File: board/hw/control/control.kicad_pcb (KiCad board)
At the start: 2 copper layers, 54.3 x 82.5 mm, 40 parts, among them T1 pn2222a, T2 pn2222a, T3 pn2222a, T4 pn2222a, T5 pn2222a, T6 pn2222a, T7 pn2222a, T8 pn2222a

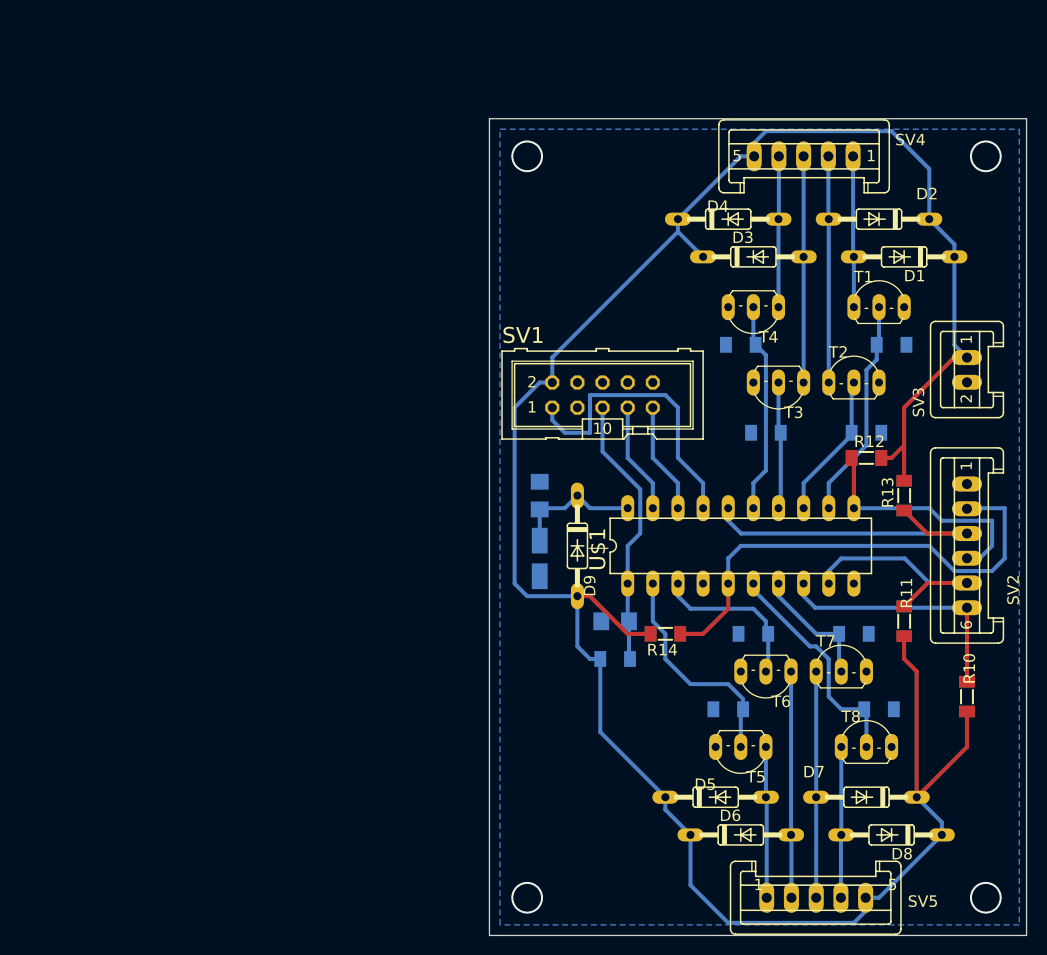
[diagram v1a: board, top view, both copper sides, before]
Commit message: moved most elements from Eagle to KiCad libraries
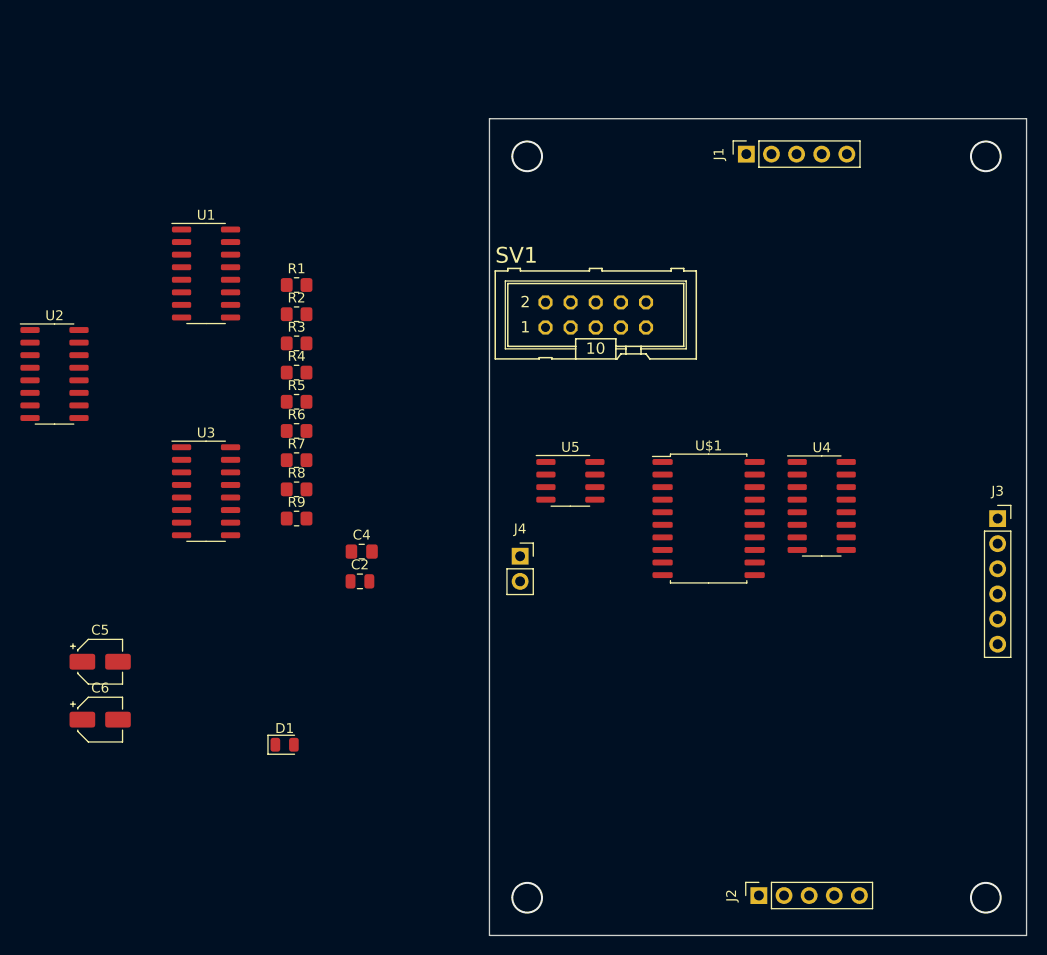
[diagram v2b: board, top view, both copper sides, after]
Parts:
- removed C3: 4.7uF, control:153CLV-0405
- removed D2, D3, D4, D5, D6, D7, D8, D9: 1N4446, control:DO35-10
- removed R10, R11, R12, R13, R14: 100kR, control:MINI_MELF-0204W
- removed SV2: buttons, control:S06P
- removed SV3: , control:S02P
- removed SV4: stepper #1, control:S05P
- removed SV5: stepper #2, control:S05P
- removed T1, T2, T3, T4, T5, T6, T7, T8: pn2222a, control:TO92-CBE
- added C5: 4.7µF, Capacitor_SMD:CP_Elec_4x5.8, F.Cu at (82.0, 118.6)
- added C6: 4.7µF, Capacitor_SMD:CP_Elec_4x5.8, F.Cu at (82.0, 124.5)
- added J1: stepper #1, Connector_PinSocket_2.54mm:PinSocket_1x05_P2.54mm_Vertical, F.Cu at (147.3, 67.3)
- added J2: stepper #2, Connector_PinSocket_2.54mm:PinSocket_1x05_P2.54mm_Vertical, F.Cu at (148.6, 142.2)
- added J3: buttons, Connector_PinSocket_2.54mm:PinSocket_1x06_P2.54mm_Vertical, F.Cu at (172.7, 104.1)
- added J4: power, Connector_PinSocket_2.54mm:PinSocket_1x02_P2.54mm_Vertical, F.Cu at (124.5, 108.0)
- added U1: ULN2003A, Package_SO:SOIC-16_3.9x9.9mm_P1.27mm, F.Cu at (92.7, 79.4)
- added U2: ULN2003A, Package_SO:SOIC-16_3.9x9.9mm_P1.27mm, F.Cu at (77.4, 89.5)
- added U3: ULN2003A, Package_SO:SOIC-16_3.9x9.9mm_P1.27mm, F.Cu at (92.7, 101.4)
- added U4: ULN2003A, Package_SO:SOIC-16_3.9x9.9mm_P1.27mm, F.Cu at (154.9, 102.9)
- added U5: LM78L05_SO8, Package_SO:SOIC-8_3.9x4.9mm_P1.27mm, F.Cu at (129.5, 100.3)
- C2: footprint control:C3216 -> Capacitor_SMD:C_0805_2012Metric; moved to F.Cu
- C4: footprint control:C3216 -> Capacitor_SMD:C_0805_2012Metric_Pad1.18x1.45mm_HandSolder; moved to F.Cu
- D1: value 1N4446 -> TS418C; footprint control:DO35-10 -> Diode_SMD:D_0805_2012Metric
- R1, R2, R3, R4, R5, R6, R7, R8, R9: footprint control:MINI_MELF-0204W -> Resistor_SMD:R_0805_2012Metric_Pad1.20x1.40mm_HandSolder; moved to F.Cu
- U$1: footprint control:DIL20 -> Package_SO:SOIC-20W_7.5x12.8mm_P1.27mm
- moved D1 79.7 mm to (100.7, 127.0), turned to 0 degrees
- moved R9 61.9 mm to (101.9, 104.1), turned to 0 degrees
- moved R1 60.4 mm to (101.9, 80.5), turned to 0 degrees
- moved R3 58.3 mm to (101.9, 86.4), turned to 0 degrees
- moved R8 58.2 mm to (101.9, 101.2), turned to 0 degrees
- moved R6 51.9 mm to (101.9, 95.3)
- moved R7 49.4 mm to (101.9, 98.2)
- moved R4 47.8 mm to (101.9, 89.4)
- moved R2 47.4 mm to (101.9, 83.5), turned to 0 degrees
- moved R5 45.3 mm to (101.9, 92.3)
- moved C2 26.1 mm to (108.3, 110.5), turned to 0 degrees
- moved C4 18.9 mm to (108.5, 107.5), turned to 0 degrees
- moved SV1 8.13 mm to (132.1, 83.6)
- moved U$1 4.27 mm to (143.5, 104.1)
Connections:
- U$1 pad 4: (no net) -> unconnected-(U$1-PA1(XTAL2)-Pad4)
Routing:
- net +5V: track 233.1 -> 0.00 mm
- net Net-(J3-Pin_6): track 49.9 -> 0.00 mm
- net Net-(J3-Pin_5): track 33.2 -> 0.00 mm
- net Net-(U$1-(MOSI)PB5): track 30.0 -> 0.00 mm
- net Net-(U$1-PA2(/RESET)): track 27.6 -> 0.00 mm
- net Net-(J3-Pin_2): track 25.8 -> 0.00 mm
- net Net-(J3-Pin_4): track 25.3 -> 0.00 mm
- net Net-(J3-Pin_3): track 24.1 -> 0.00 mm
- net Net-(U$1-(INT0)PD2): track 23.0 -> 0.00 mm
- net N$10: track 22.9 -> 0.00 mm
- net N$21: track 22.9 -> 0.00 mm
- net N$5: track 22.9 -> 0.00 mm
- net N$12: track 22.9 -> 0.00 mm
- net Net-(U$1-(RXD)PD0): track 22.6 -> 0.00 mm
- net Net-(U$1-(AIN0)PB0): track 22.4 -> 0.00 mm
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- removed copper zone on B.Cu, net 0V
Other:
- board text removed: "+5V"
- board text removed: "GND"

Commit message: removed unused elements and added proper AVR-ISP-10 conector
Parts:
- removed SV1: KANDA, control:ML10
- added J6: AVR-ISP-10, Connector_IDC:IDC-Header_2x05_P2.54mm_Vertical, F.Cu at (134.6, 86.4)
- J1, J2: footprint Connector_PinSocket_2.54mm:PinSocket_1x05_P2.54mm_Vertical -> Connector_PinHeader_2.54mm:PinHeader_1x05_P2.54mm_Vertical
- J4: footprint Connector_PinSocket_2.54mm:PinSocket_1x02_P2.54mm_Vertical -> Connector_PinHeader_2.54mm:PinHeader_1x02_P2.54mm_Vertical

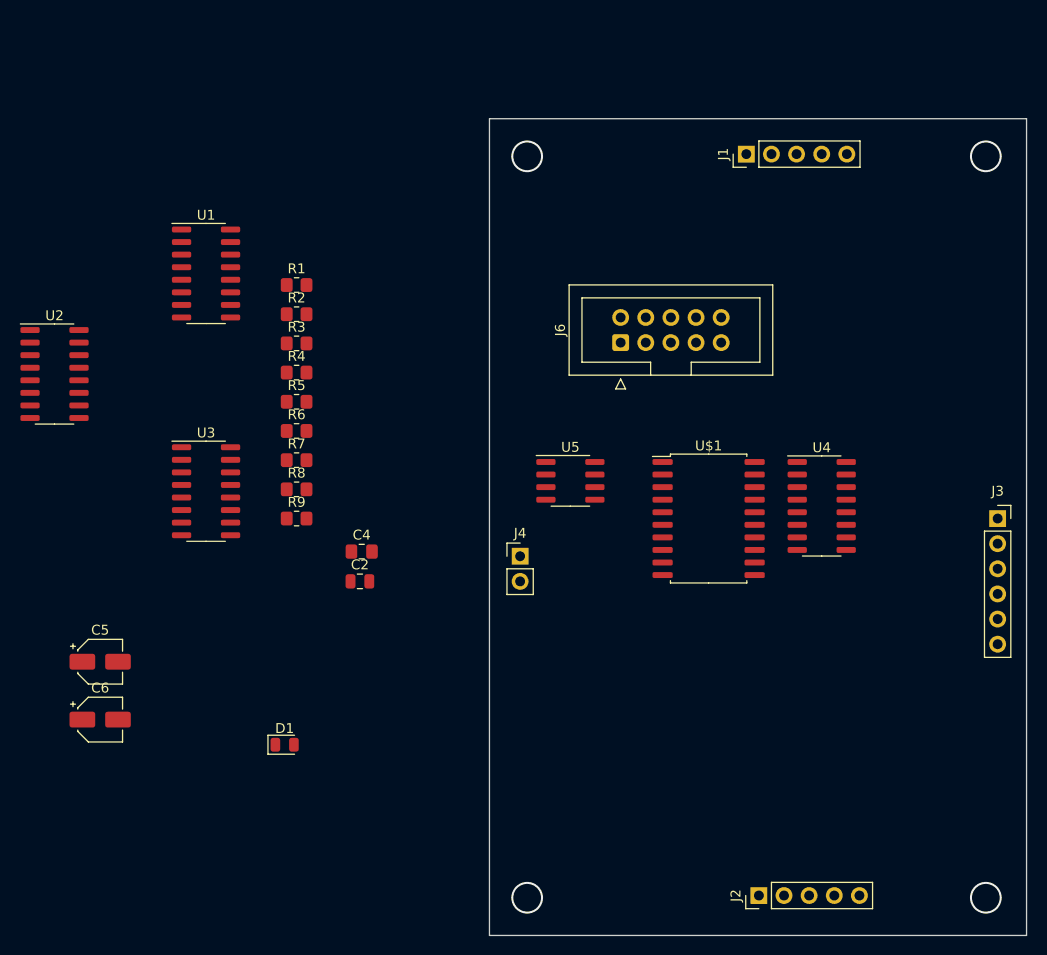
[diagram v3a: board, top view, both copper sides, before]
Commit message: assigned correct sizes of elements + some draft positioning; still need to add power management cirtcuitry
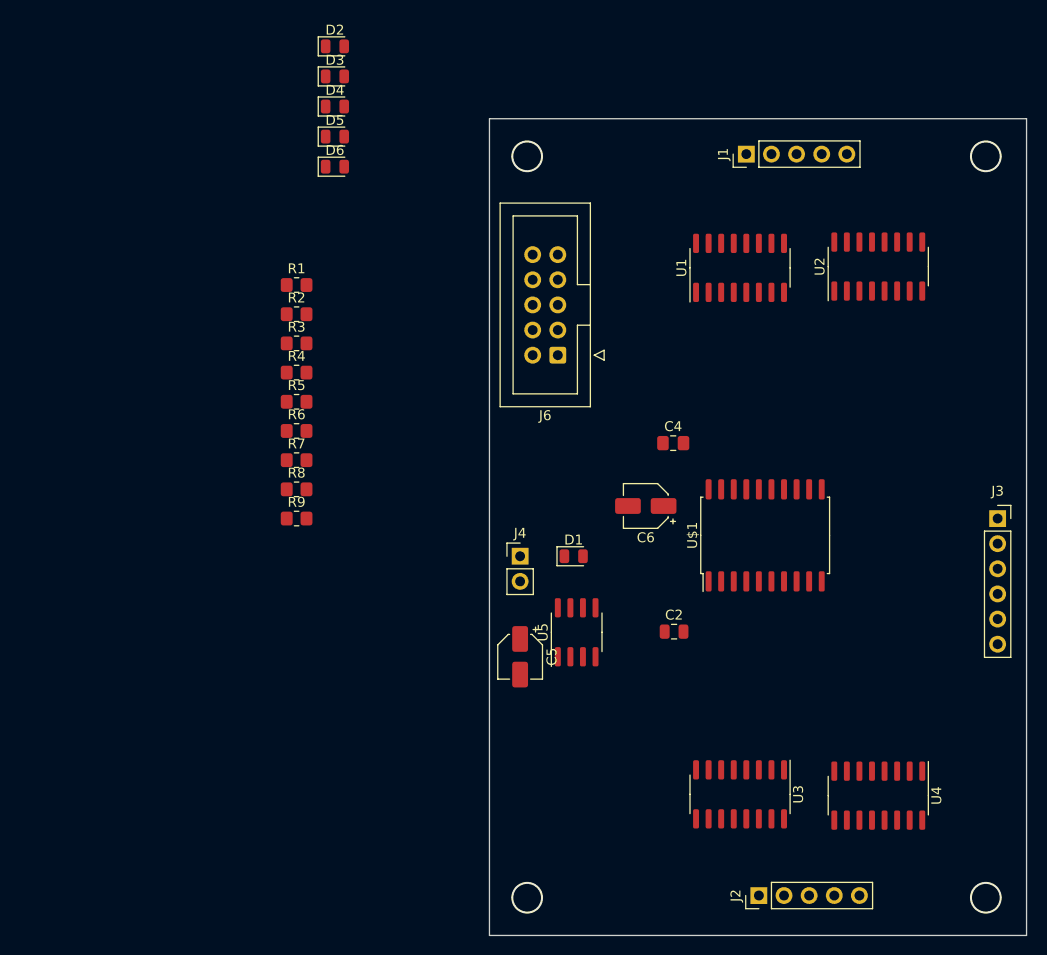
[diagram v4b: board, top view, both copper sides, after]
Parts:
- added D2: TS418C, Diode_SMD:D_0805_2012Metric, F.Cu at (105.7, 56.4)
- added D3: TS418C, Diode_SMD:D_0805_2012Metric, F.Cu at (105.7, 59.5)
- added D4: TS418C, Diode_SMD:D_0805_2012Metric, F.Cu at (105.7, 62.5)
- added D5: TS418C, Diode_SMD:D_0805_2012Metric, F.Cu at (105.7, 65.5)
- added D6: TS418C, Diode_SMD:D_0805_2012Metric, F.Cu at (105.7, 68.6)
- moved U2 84.0 mm to (160.7, 78.7), turned to 90 degrees
- moved U3 62.1 mm to (146.7, 132.0), turned to -90 degrees
- moved C6 59.2 mm to (137.2, 102.9), turned to 180 degrees
- moved U1 54.0 mm to (146.7, 78.8), turned to 90 degrees
- moved C5 42.4 mm to (124.5, 118.1), turned to -90 degrees
- moved D1 34.9 mm to (129.9, 108.0)
- moved C4 33.3 mm to (139.9, 96.5)
- moved C2 32.2 mm to (140.0, 115.6)
- moved U4 29.8 mm to (160.7, 132.1), turned to -90 degrees
- moved U5 15.3 mm to (130.2, 115.6), turned to 90 degrees
- moved J6 6.48 mm to (128.3, 87.6), turned to 180 degrees
- moved U$1 5.96 mm to (149.2, 105.8), turned to 90 degrees
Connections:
- J3 pad 2: Net-(J3-Pin_2) -> Net-(D6-K)
- J3 pad 3: Net-(J3-Pin_3) -> Net-(D5-K)
- J3 pad 4: Net-(J3-Pin_4) -> Net-(D4-K)
- J3 pad 5: Net-(J3-Pin_5) -> Net-(D3-K)
- J3 pad 6: Net-(J3-Pin_6) -> Net-(D2-K)
- U$1 pad 11: Net-(J3-Pin_4) -> Net-(D4-A)
- U$1 pad 16: Net-(J3-Pin_5) -> Net-(D3-A)
- U$1 pad 5: Net-(J3-Pin_6) -> Net-(D2-A)
- U$1 pad 8: Net-(J3-Pin_2) -> Net-(D6-A)
- U$1 pad 9: Net-(J3-Pin_3) -> Net-(D5-A)

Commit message: added p-mosfet and zerenrs for power ctrl via buttons, too
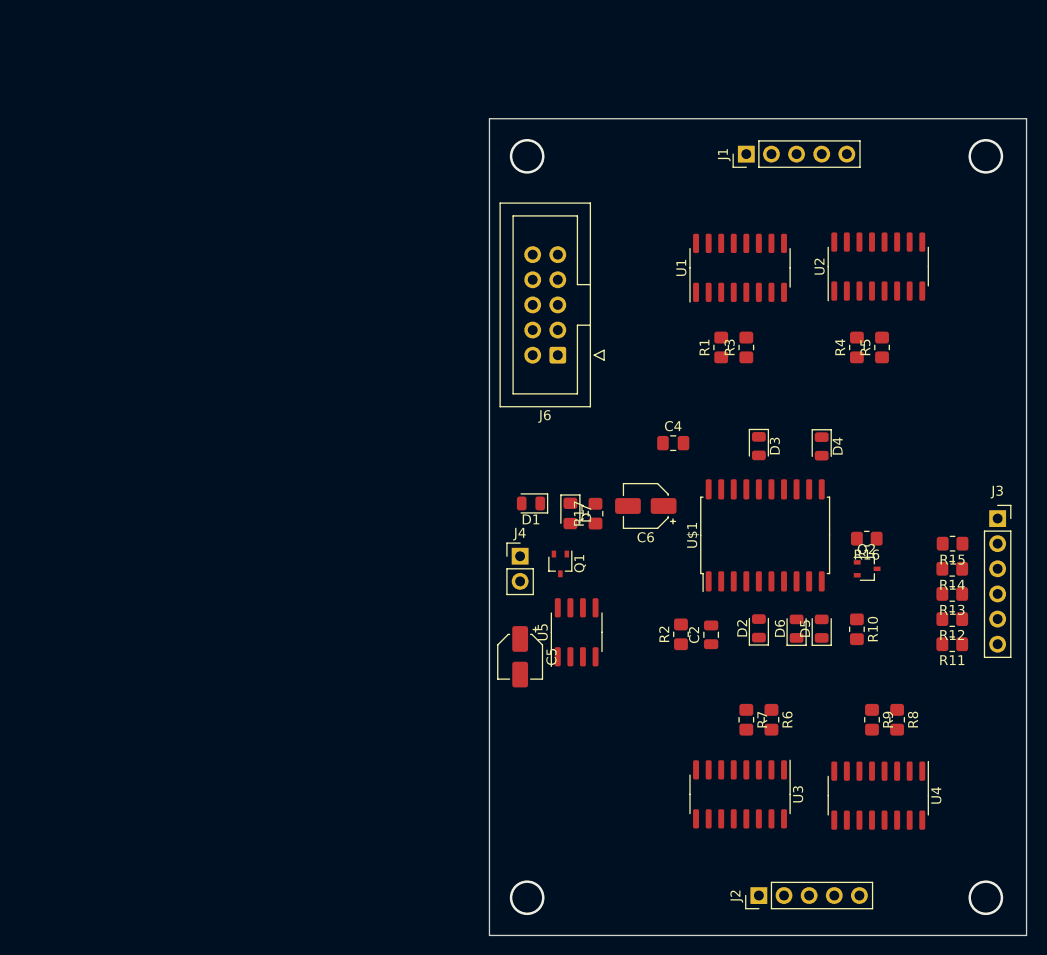
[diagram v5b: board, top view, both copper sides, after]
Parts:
- added D7: BZY55B3v0-RYG, Diode_SMD:D_0805_2012Metric_Pad1.15x1.40mm_HandSolder, F.Cu at (129.5, 103.6)
- added Q1: MMFTP84W, Package_TO_SOT_SMD:SOT-323_SC-70, F.Cu at (128.5, 108.7)
- added Q2: MMFTP84W, Package_TO_SOT_SMD:SOT-323_SC-70, F.Cu at (159.5, 109.2)
- added R10: 10kR, Resistor_SMD:R_0805_2012Metric_Pad1.20x1.40mm_HandSolder, F.Cu at (158.5, 115.3)
- added R11: 10kR, Resistor_SMD:R_0805_2012Metric_Pad1.20x1.40mm_HandSolder, F.Cu at (168.1, 116.8)
- added R12: 10kR, Resistor_SMD:R_0805_2012Metric_Pad1.20x1.40mm_HandSolder, F.Cu at (168.1, 114.3)
- added R13: 10kR, Resistor_SMD:R_0805_2012Metric_Pad1.20x1.40mm_HandSolder, F.Cu at (168.1, 111.8)
- added R14: 10kR, Resistor_SMD:R_0805_2012Metric_Pad1.20x1.40mm_HandSolder, F.Cu at (168.1, 109.2)
- added R15: 10kR, Resistor_SMD:R_0805_2012Metric_Pad1.20x1.40mm_HandSolder, F.Cu at (168.2, 106.7)
- added R16: 100kR, Resistor_SMD:R_0805_2012Metric_Pad1.20x1.40mm_HandSolder, F.Cu at (159.5, 106.2)
- added R17: 100kR, Resistor_SMD:R_0805_2012Metric_Pad1.20x1.40mm_HandSolder, F.Cu at (132.1, 103.6)
- moved D2 72.8 mm to (148.6, 115.2), turned to 90 degrees
- moved D5 70.0 mm to (154.9, 115.3), turned to 90 degrees
- moved D6 66.0 mm to (152.4, 115.3), turned to 90 degrees
- moved R8 65.0 mm to (162.6, 124.5), turned to -90 degrees
- moved R9 61.6 mm to (160.0, 124.5), turned to -90 degrees
- moved D4 60.0 mm to (154.9, 96.9), turned to -90 degrees
- moved R5 59.4 mm to (161.0, 86.9), turned to 90 degrees
- moved D3 56.8 mm to (148.6, 96.8), turned to -90 degrees
- moved R4 56.7 mm to (158.5, 86.9), turned to 90 degrees
- moved R6 56.2 mm to (149.9, 124.5), turned to -90 degrees
- moved R7 52.5 mm to (147.3, 124.5), turned to -90 degrees
- moved R2 50.6 mm to (140.7, 115.8), turned to 90 degrees
- moved R3 45.5 mm to (147.3, 86.9), turned to 90 degrees
- moved R1 43.4 mm to (144.8, 86.9), turned to 90 degrees
- moved D1 6.86 mm to (125.6, 102.6), turned to 180 degrees
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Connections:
- C5 pad 1: Net-(D1-K) -> Net-(Q1-D)
- U$1 pad 4: unconnected-(U$1-PA1(XTAL2)-Pad4) -> Net-(Q2-G)
- U5 pad 8: Net-(D1-K) -> Net-(Q1-D)
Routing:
- net 0V: vias 0 -> 4
- net (no net): vias 4 -> 0

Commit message: PCB routing mostly done - DRC is WIP
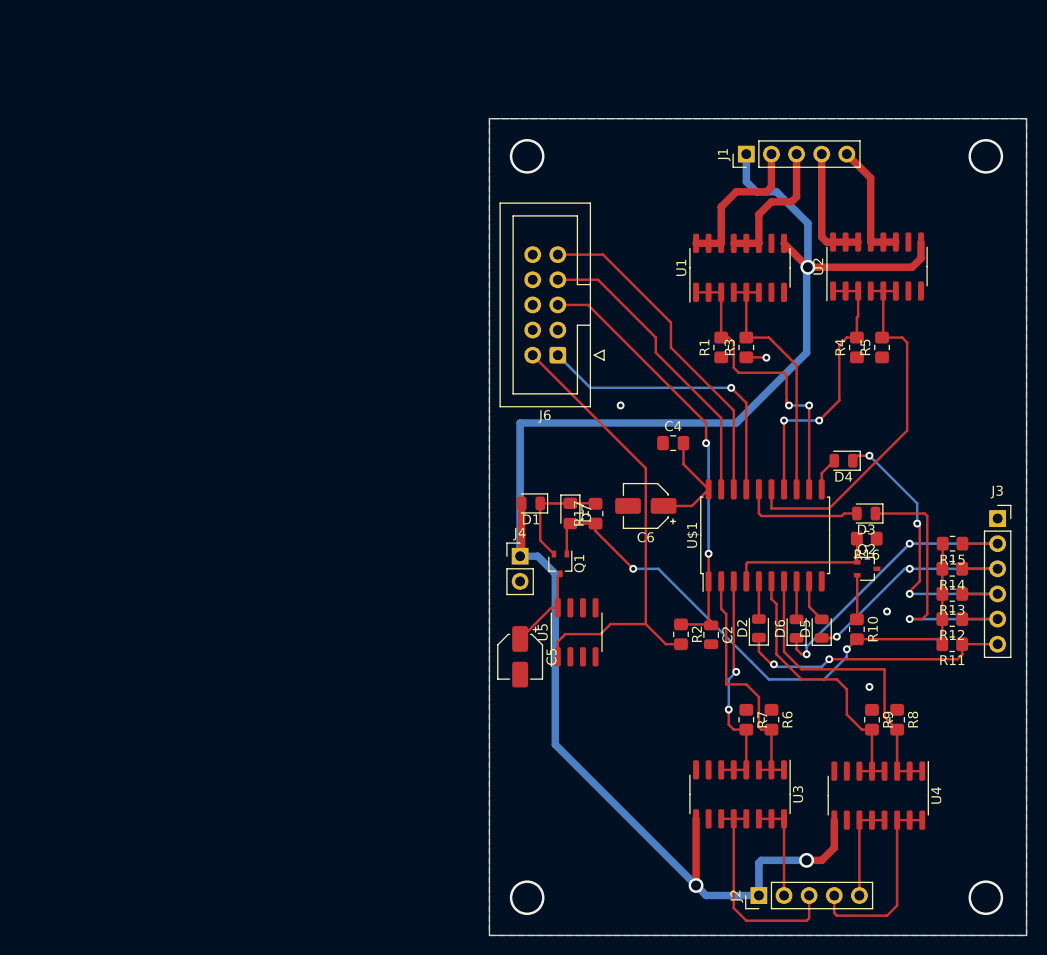
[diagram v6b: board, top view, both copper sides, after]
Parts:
- moved D3 12.8 mm to (159.4, 103.6), turned to 180 degrees
- moved D4 2.64 mm to (157.1, 98.3), turned to 180 degrees
- moved U2 0.13 mm to (160.5, 78.7)
- turned C2 to -90 degrees
- turned R2 to -90 degrees
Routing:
- net +24V: track 0.00 -> 161.0 mm, vias 0 -> 3
- net Net-(D7-A): track 0.00 -> 61.0 mm, vias 0 -> 2
- net +5V: track 0.00 -> 47.5 mm
- net Net-(J6-~{RST}): track 0.00 -> 43.7 mm, vias 0 -> 2
- net Net-(U$1-(OC1A)PB3): track 0.00 -> 37.8 mm
- net Net-(J6-MISO): track 0.00 -> 33.8 mm
- net Net-(U$1-(INT1)PD3): track 0.00 -> 31.4 mm
- net Net-(D4-K): track 0.00 -> 30.9 mm, vias 0 -> 3
- net Net-(U$1-(AIN0)PB0): track 0.00 -> 30.4 mm, vias 0 -> 2
- net Net-(J6-SCK): track 0.00 -> 30.4 mm
- net Net-(D6-K): track 0.00 -> 30.3 mm, vias 0 -> 2
- net Net-(J6-MOSI): track 0.00 -> 29.8 mm, vias 0 -> 1
- net Net-(D3-K): track 0.00 -> 29.7 mm, vias 0 -> 1
- net Net-(U$1-(INT0)PD2): track 0.00 -> 28.6 mm
- net Net-(U$1-(OC0A)PB2): track 0.00 -> 28.4 mm, vias 0 -> 2
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- added copper zone on B.Cu, net 0V
- added copper zone on F.Cu, net 0V
